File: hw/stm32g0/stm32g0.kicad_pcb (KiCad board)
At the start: 4 copper layers, 80 x 40 mm, 74 parts, among them J101 Barrel_Jack_Switch, J102 Screw_Terminal_01x03, J201 Conn_01x06, J202 Conn_01x04, J203 Conn_01x05, Q101 BC817, SW401 SW_Push, SW402 SW_Push, SW403 SW_Push, SW404 SW_Push, SW405 SW_Push, SW406 SW_Push, U201 STM32G030K8Tx, U202 74AHCT125, U203 CAT24C256, U301 VS1838B, U401 4050, U501 AMS1117-3.3

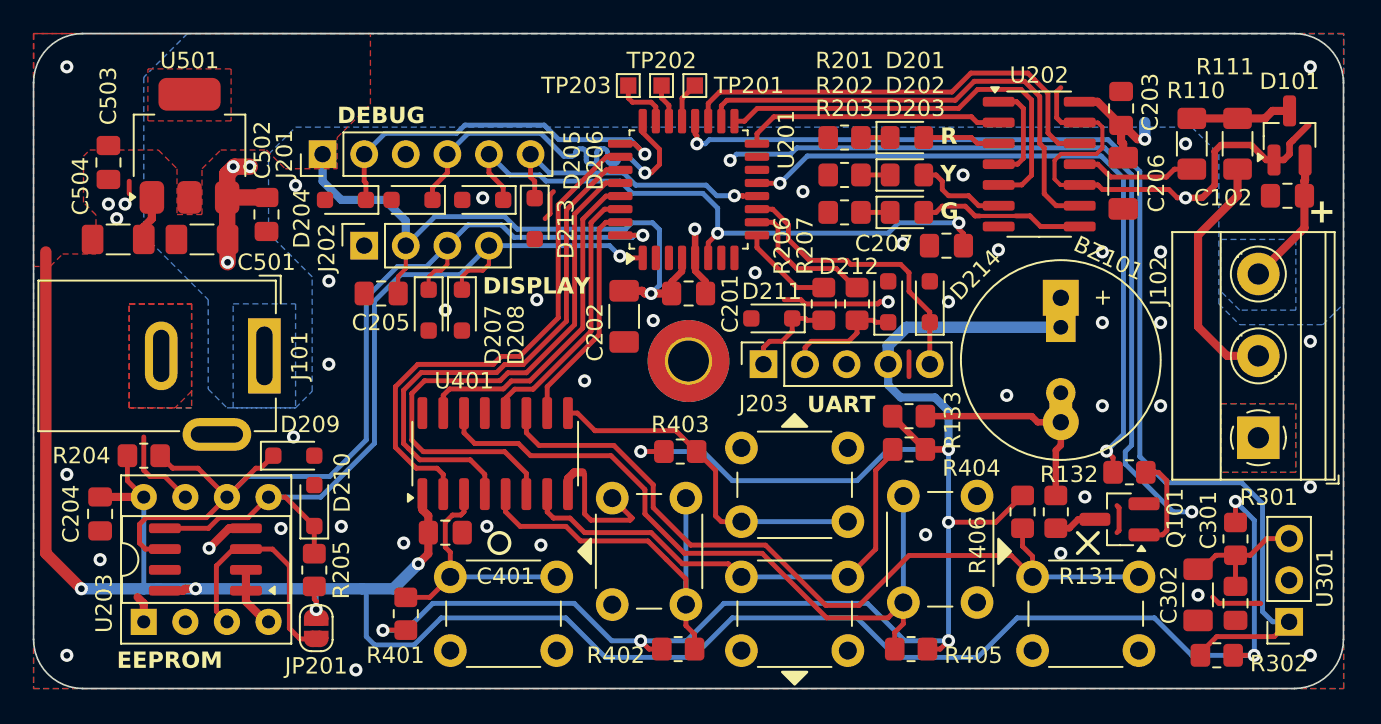
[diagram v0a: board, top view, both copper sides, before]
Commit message: chore(hw): move test points
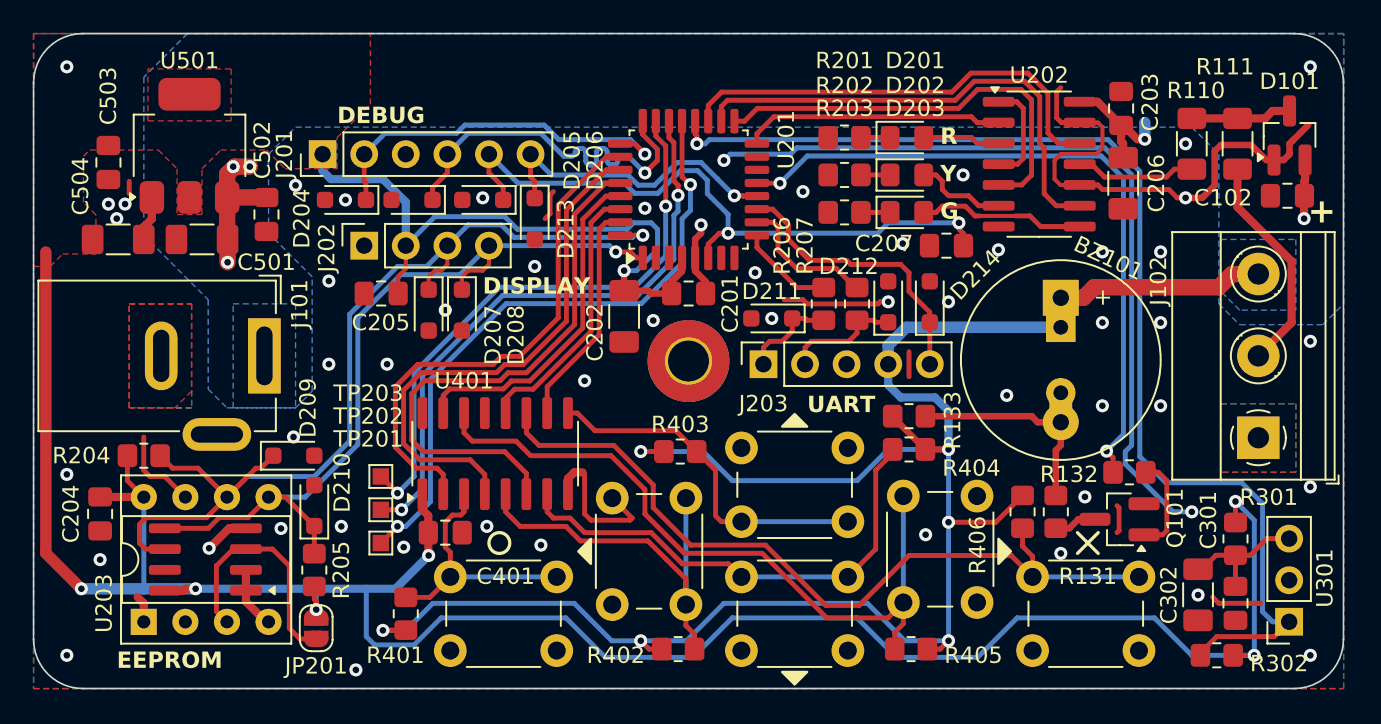
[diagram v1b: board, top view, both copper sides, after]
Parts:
- moved TP201 33.9 mm to (140.6, 106.0)
- moved TP202 31.1 mm to (140.6, 104.0)
- moved TP203 28.3 mm to (140.6, 102.0)
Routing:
- net /CPU/DEBUG_1: track 2.50 -> 39.0 mm, vias 0 -> 2
- net /CPU/DEBUG_2: track 2.36 -> 37.1 mm, vias 0 -> 2
- net /CPU/DEBUG_3: track 3.54 -> 36.0 mm, vias 0 -> 2
- net +5V: track 143.6 -> 139.0 mm, vias 10 -> 11
- net /CPU/~{RESET}: track 38.3 -> 40.3 mm
- net Net-(J102-Pin_2): track 15.0 -> 13.6 mm
- net +3.3V: track 177.6 -> 178.8 mm
- net /CPU/DBG_SPARE: track 17.7 -> 18.8 mm
- net GND: track 131.8 -> 132.5 mm, vias 50 -> 54
- net /CPU/I2C_SDA: track 51.6 -> 50.9 mm
- net /CPU/I2C_SCL: track 60.4 -> 59.9 mm

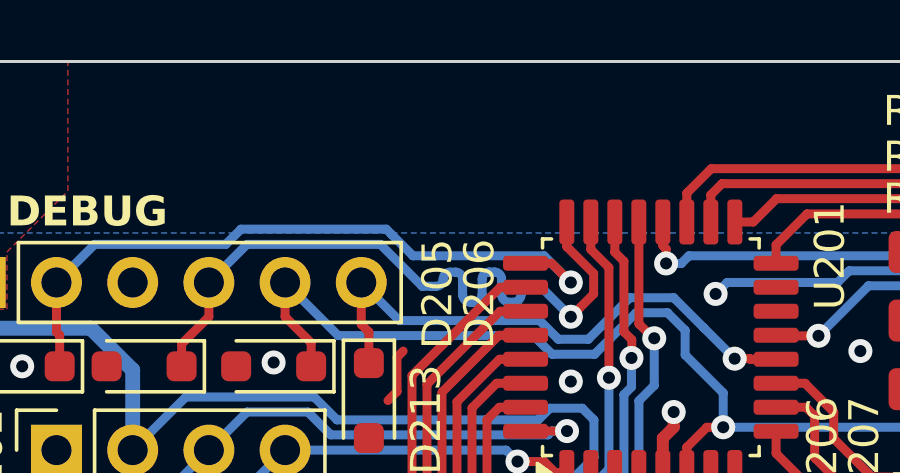
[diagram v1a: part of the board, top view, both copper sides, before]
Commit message: chore(hw): add logos
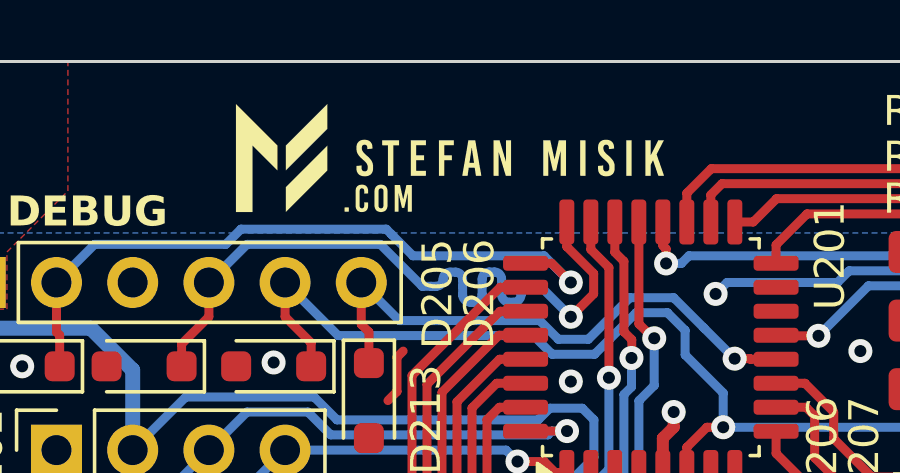
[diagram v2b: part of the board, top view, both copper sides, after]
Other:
- board text removed: "stefanmisik.com"

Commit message: chore(hw): add version number
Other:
- board text added: "v3.0"
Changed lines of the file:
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@@
+		)
+	)
+	(gr_text "v3.0"
+		(at 143.256 99.314 90)
+		(layer "B.SilkS")
+		(effects
+			(font
+				(size 1 1)
+				(thickness 0.15)
+			)
+			(justify left bottom mirror)
 		)
 	)

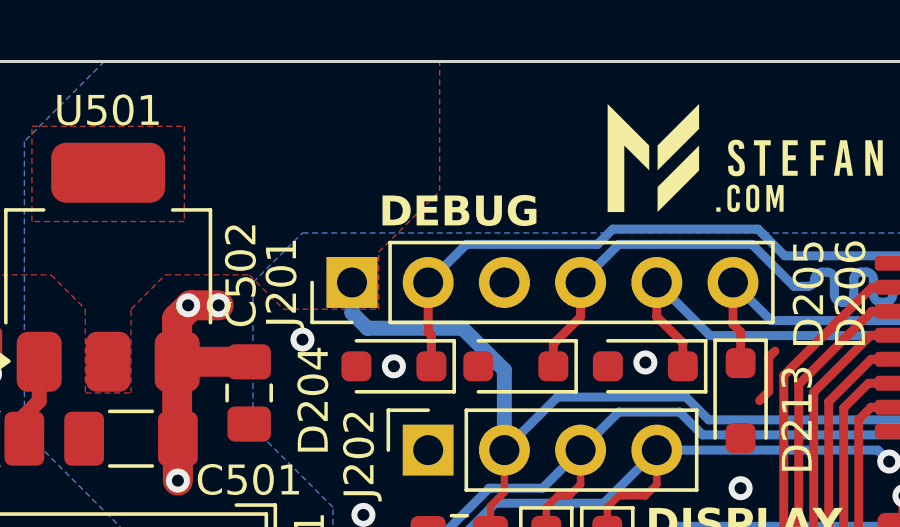
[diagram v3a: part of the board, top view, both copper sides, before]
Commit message: chore(hw): improve debug port silkscreen marks
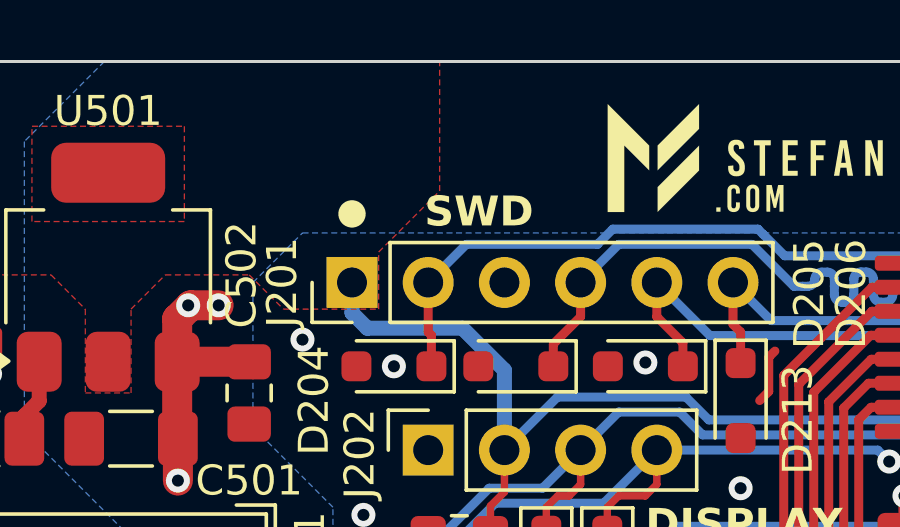
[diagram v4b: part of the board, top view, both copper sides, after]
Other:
- board text added: "SWD"
- board text removed: "DEBUG"
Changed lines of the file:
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@@
+		(layer "F.SilkS")
+	)
+	(gr_circle
+		(center 137.033 80.01)
+		(end 137.414 80.01)
+		(stroke
+			(width 0.15)
+			(type solid)
+		)
+		(fill solid)
 		(layer "F.SilkS")
 	)
@@
 		)
 	)
-	(gr_text "DEBUG"
-		(at 137.922 80.518 0)
+	(gr_text "SWD"
+		(at 139.446 80.518 0)
 		(layer "F.SilkS")
 		(effects

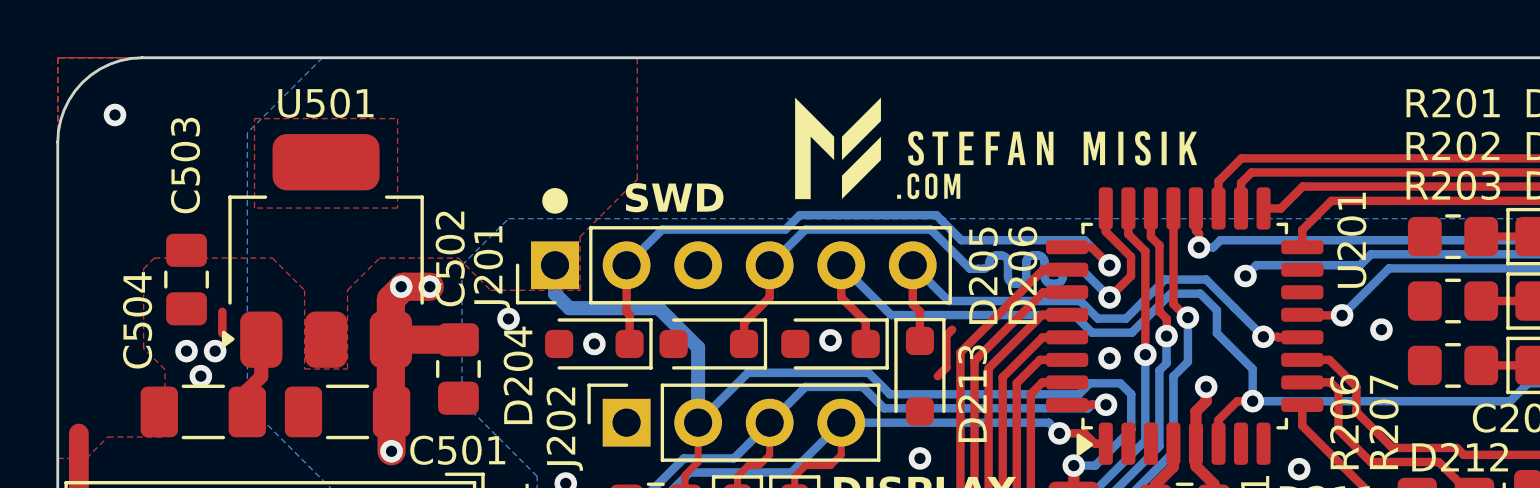
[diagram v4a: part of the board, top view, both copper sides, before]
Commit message: chore(hw): add debug port resistors
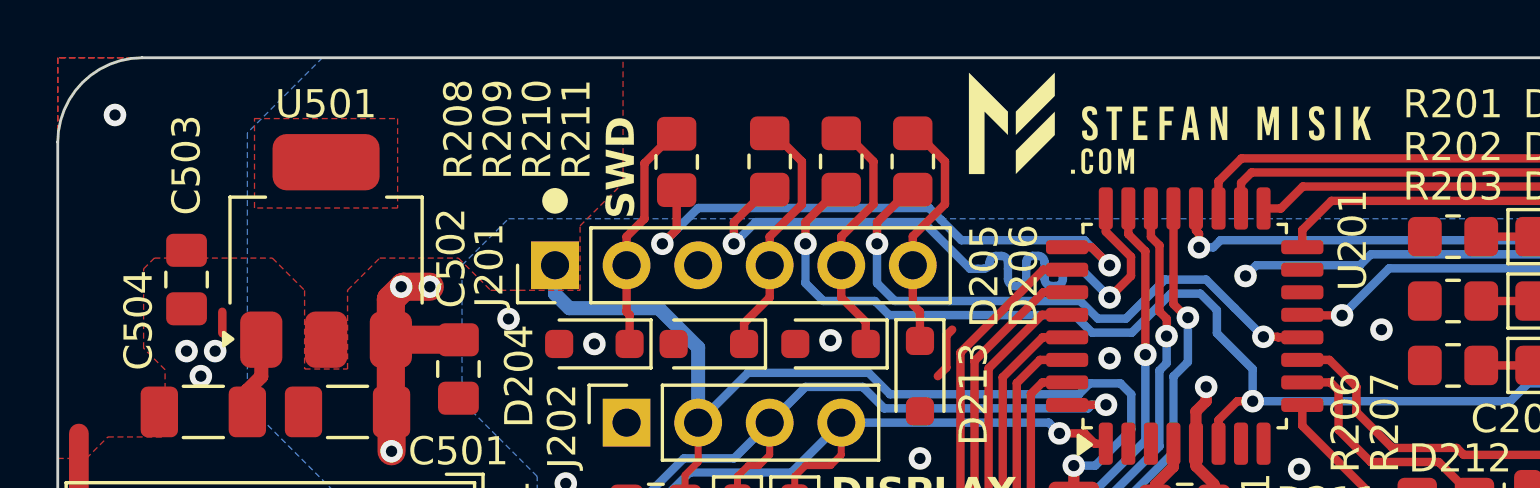
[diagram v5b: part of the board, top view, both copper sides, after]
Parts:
- added R208: 33R, Resistor_SMD:R_0805_2012Metric_Pad1.20x1.40mm_HandSolder, F.Cu at (141.4, 78.6)
- added R209: 33R, Resistor_SMD:R_0805_2012Metric_Pad1.20x1.40mm_HandSolder, F.Cu at (144.7, 78.6)
- added R210: 33R, Resistor_SMD:R_0805_2012Metric_Pad1.20x1.40mm_HandSolder, F.Cu at (147.2, 78.6)
- added R211: 33R, Resistor_SMD:R_0805_2012Metric_Pad1.20x1.40mm_HandSolder, F.Cu at (149.7, 78.6)
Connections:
- D204 pad 1: /CPU/SWCLK -> Net-(D204-A1)
- D205 pad 1: /CPU/SWDIO -> Net-(D205-A1)
- D206 pad 1: /CPU/~{RESET} -> Net-(D206-A1)
- D213 pad 1: /CPU/DBG_SPARE -> Net-(D213-A1)
- J201 pad 2: /CPU/SWCLK -> Net-(D204-A1)
- J201 pad 4: /CPU/SWDIO -> Net-(D205-A1)
- J201 pad 5: /CPU/~{RESET} -> Net-(D206-A1)
- J201 pad 6: /CPU/DBG_SPARE -> Net-(D213-A1)
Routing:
- net Net-(D205-A1): track 0.00 -> 8.88 mm
- net Net-(D206-A1): track 0.00 -> 8.87 mm
- net Net-(D213-A1): track 0.00 -> 8.51 mm
- net Net-(D204-A1): track 0.00 -> 8.30 mm
- net /CPU/DBG_SPARE: track 18.8 -> 21.0 mm, vias 1 -> 2
- net /CPU/SWCLK: track 23.2 -> 21.1 mm, vias 1 -> 2
- net /CPU/~{RESET}: track 40.3 -> 42.0 mm, vias 2 -> 3
- net /CPU/SWDIO: track 23.5 -> 24.2 mm, vias 1 -> 2

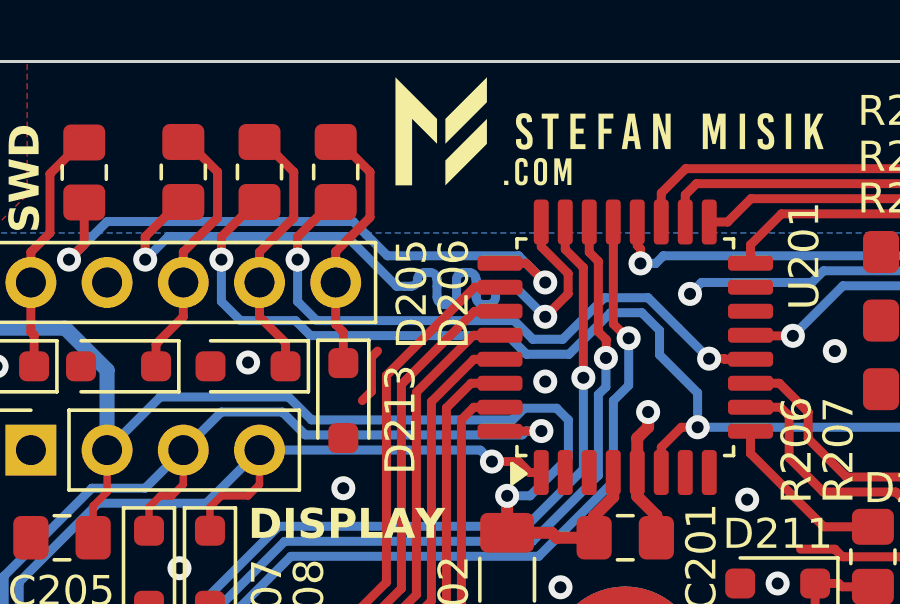
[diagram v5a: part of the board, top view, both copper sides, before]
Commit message: chore(hw): fix debug port meander
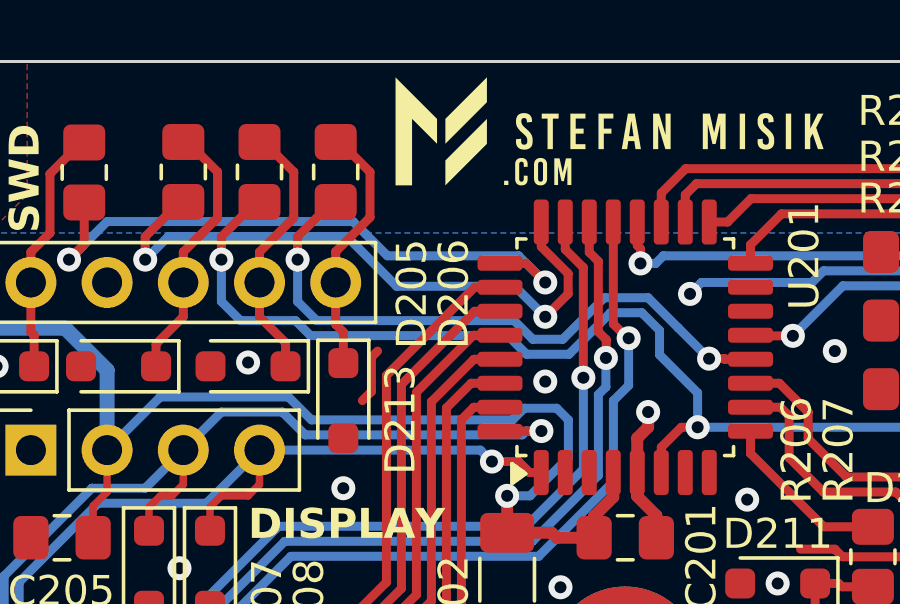
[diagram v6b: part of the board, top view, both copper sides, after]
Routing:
- net /CPU/SWDIO: track 24.2 -> 21.1 mm
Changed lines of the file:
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@@
 	)
 	(segment
-		(start 154.801 83.033976)
-		(end 154.671 83.033976)
-		(width 0.3)
-		(layer "B.Cu")
-		(net 15)
-	)
-	(segment
-		(start 156.718 83.439)
-		(end 155.702 82.423)
-		(width 0.3)
-		(layer "B.Cu")
-		(net 15)
-	)
-	(segment
-		(start 153.111 82.423)
-		(end 153.111 82.194641)
-		(width 0.3)
-		(layer "B.Cu")
-		(net 15)
-	)
-	(segment
 		(start 155.702 82.423)
 		(end 155.321 82.423)
@@
 	)
 	(segment
-		(start 155.061 82.683)
-		(end 155.061 82.773976)
-		(width 0.3)
-		(layer "B.Cu")
-		(net 15)
-	)
-	(segment
-		(start 153.501 83.033976)
-		(end 153.371 83.033976)
-		(width 0.3)
-		(layer "B.Cu")
-		(net 15)
-	)
-	(segment
-		(start 152.882641 81.966282)
-		(end 152.689359 81.966282)
-		(width 0.3)
-		(layer "B.Cu")
-		(net 15)
-	)
-	(segment
-		(start 152.046 82.423)
-		(end 151.765 82.423)
-		(width 0.3)
-		(layer "B.Cu")
-		(net 15)
-	)
-	(segment
-		(start 154.181728 81.964456)
-		(end 153.990272 81.964456)
-		(width 0.3)
-		(layer "B.Cu")
-		(net 15)
-	)
-	(segment
-		(start 154.411 82.423)
-		(end 154.411 82.193728)
+		(start 151.765 82.423)
+		(end 150.106 80.764)
 		(width 0.3)
 		(layer "B.Cu")
@@
 	)
 	(segment
-		(start 152.232641 82.423)
-		(end 152.046 82.423)
-		(width 0.3)
-		(layer "B.Cu")
-		(net 15)
-	)
-	(segment
-		(start 153.761 82.423)
-		(end 153.761 82.773976)
-		(width 0.3)
-		(layer "B.Cu")
-		(net 15)
-	)
-	(segment
-		(start 154.411 82.683)
-		(end 154.411 82.423)
-		(width 0.3)
-		(layer "B.Cu")
-		(net 15)
-	)
-	(segment
-		(start 153.111 82.773976)
-		(end 153.111 82.423)
-		(width 0.3)
-		(layer "B.Cu")
-		(net 15)
-	)
-	(segment
-		(start 151.765 82.423)
-		(end 150.106 80.764)
-		(width 0.3)
-		(layer "B.Cu")
-		(net 15)
-	)
-	(segment
-		(start 153.761 82.193728)
-		(end 153.761 82.423)
+		(start 156.718 83.439)
+		(end 155.702 82.423)
 		(width 0.3)
 		(layer "B.Cu")
@@
 	)
 	(segment
-		(start 154.411 82.773976)
-		(end 154.411 82.683)
-		(width 0.3)
-		(layer "B.Cu")
-		(net 15)
-	)
-	(arc
-		(start 153.371 83.033976)
-		(mid 153.187152 82.957824)
-		(end 153.111 82.773976)
-		(width 0.3)
-		(layer "B.Cu")
-		(net 15)
-	)
-	(arc
 		(start 155.321 82.423)
-		(mid 155.137152 82.499152)
-		(end 155.061 82.683)
-		(width 0.3)
-		(layer "B.Cu")
-		(net 15)
-	)
-	(arc
-		(start 153.990272 81.964456)
-		(mid 153.828152 82.031608)
-		(end 153.761 82.193728)
-		(width 0.3)
-		(layer "B.Cu")
-		(net 15)
-	)
-	(arc
-		(start 154.671 83.033976)
-		(mid 154.487152 82.957824)
-		(end 154.411 82.773976)
-		(width 0.3)
-		(layer "B.Cu")
-		(net 15)
-	)
-	(arc
-		(start 152.689359 81.966282)
-		(mid 152.527885 82.033167)
-		(end 152.461 82.194641)
-		(width 0.3)
-		(layer "B.Cu")
-		(net 15)
-	)
-	(arc
-		(start 153.111 82.194641)
-		(mid 153.044115 82.033167)
-		(end 152.882641 81.966282)
-		(width 0.3)
-		(layer "B.Cu")
-		(net 15)
-	)
-	(arc
-		(start 154.411 82.193728)
-		(mid 154.343848 82.031608)
-		(end 154.181728 81.964456)
-		(width 0.3)
-		(layer "B.Cu")
-		(net 15)
-	)
-	(arc
-		(start 155.061 82.773976)
-		(mid 154.984848 82.957824)
-		(end 154.801 83.033976)
-		(width 0.3)
-		(layer "B.Cu")
-		(net 15)
-	)
-	(arc
-		(start 153.761 82.773976)
-		(mid 153.684848 82.957824)
-		(end 153.501 83.033976)
-		(width 0.3)
-		(layer "B.Cu")
-		(net 15)
-	)
-	(arc
-		(start 152.461 82.194641)
-		(mid 152.394115 82.356115)
-		(end 152.232641 82.423)
+		(end 151.765 82.423)
 		(width 0.3)
 		(layer "B.Cu")
@@
 		(last_status "tuned")
 		(last_track_width 0.3)
-		(last_tuning "29.3000 mm (tuned)")
+		(last_tuning "24.1107 mm (tuned)")
 		(max_amplitude 0.62)
 		(min_amplitude 0.2)
@@
 		(rounded yes)
 		(single_sided no)
-		(target_length 29.3)
-		(target_length_max 29.4)
-		(target_length_min 29.2)
+		(target_length 24.15)
+		(target_length_max 24.25)
+		(target_length_min 24.05)
 		(target_skew 0)
 		(target_skew_max 0.1)
 		(target_skew_min -0.1)
 		(tuning_mode "single")
-		(members 0282f03d-388c-4b82-b7a5-279828db69f7 0e4520d1-7bc9-4a7a-80af-8b0faba0b2ea
-			247cd3cb-db85-42eb-b553-3260204f9385 35e790bf-38a1-4bc8-9222-fb4de2da0295
-			3695213b-b6cf-4644-ab14-ea1c49cc767d 3966b3ec-06c8-4b93-8d9c-4c7c82c111f3
-			50f88468-9d3a-403f-983a-51e734023b83 555e05ee-4660-468d-af95-b8b2761393ab
-			56e14f52-4fe7-4a6d-9db8-c0ef09cec6b7 59a7bec0-407b-49ba-869b-6063b440d3d1
-			62213ccb-5bfe-4ec5-a356-f7abc723820d 6492804c-bfb6-4d0a-9c22-494d2d3ac3cb
-			64ca7e5d-c509-4851-b33d-e9204247ca89 79e72bce-1336-4900-a782-2bc360a03f01
-			7f7af0f7-47fe-44d2-8083-fd82ee1a5284 7f8d3f75-62cd-41fa-9a68-6c162e49e849
-			9bb2b040-94ad-4384-98e0-fe7e80aefb85 c8c0bf9b-79fb-43ca-ae86-9399ad714caf
-			d7cdcd17-0721-4e33-919e-fe70de615f95 e19fbb30-eee5-4e1c-aba3-d09a87abeb97
-			ef2cba02-5df2-4ceb-aaaa-f38b584bfd76 f8248c30-228f-47f7-b753-4d55421d5492
-			f8423874-ef72-467a-9e3c-5a9e93ed9871 fc2958c8-eefe-4db0-842e-5274bc475f22
-		)
+		(members be427784-3c07-47aa-96af-dc3efb95d378)
 	)
 )
